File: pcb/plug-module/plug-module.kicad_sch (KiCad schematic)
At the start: 15 parts, among them J1 Conn_01x10_Pin, J2 Conn_01x04_Pin, J3 Conn_01x15_Socket, J4 Conn_01x04_Pin, J5 Conn_01x10_Pin, Q1 BS170, U1 74HC688, U2 74AHC1G08, U3 74HC595

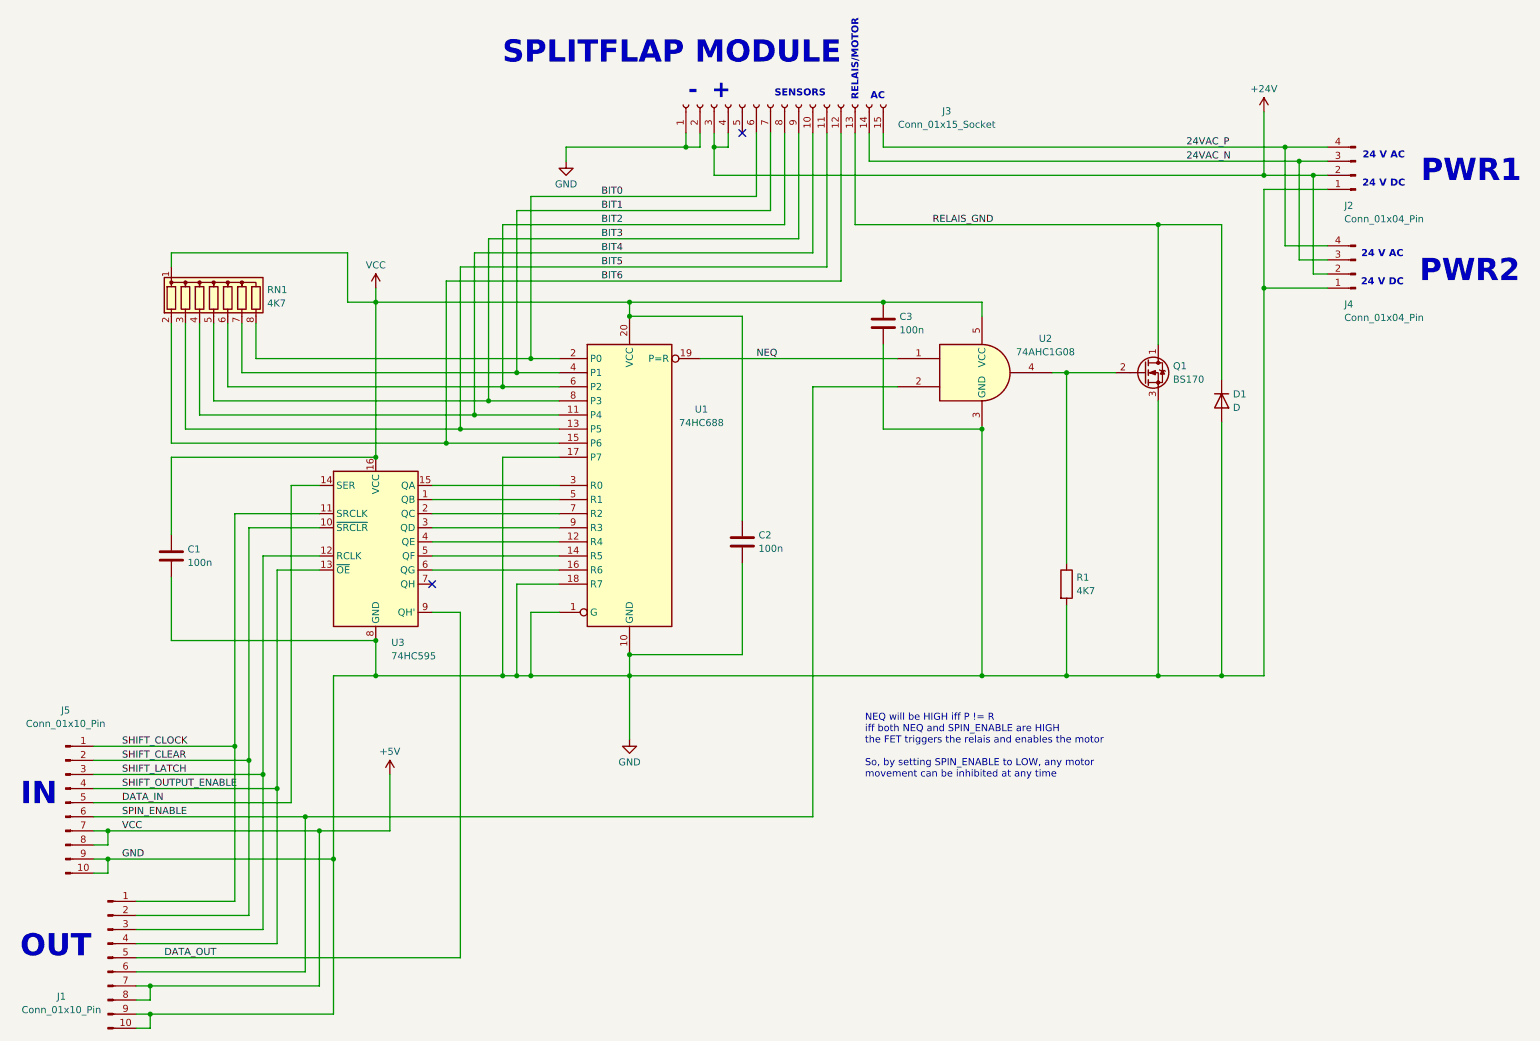
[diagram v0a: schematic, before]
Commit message: plug module improvements (soldering)
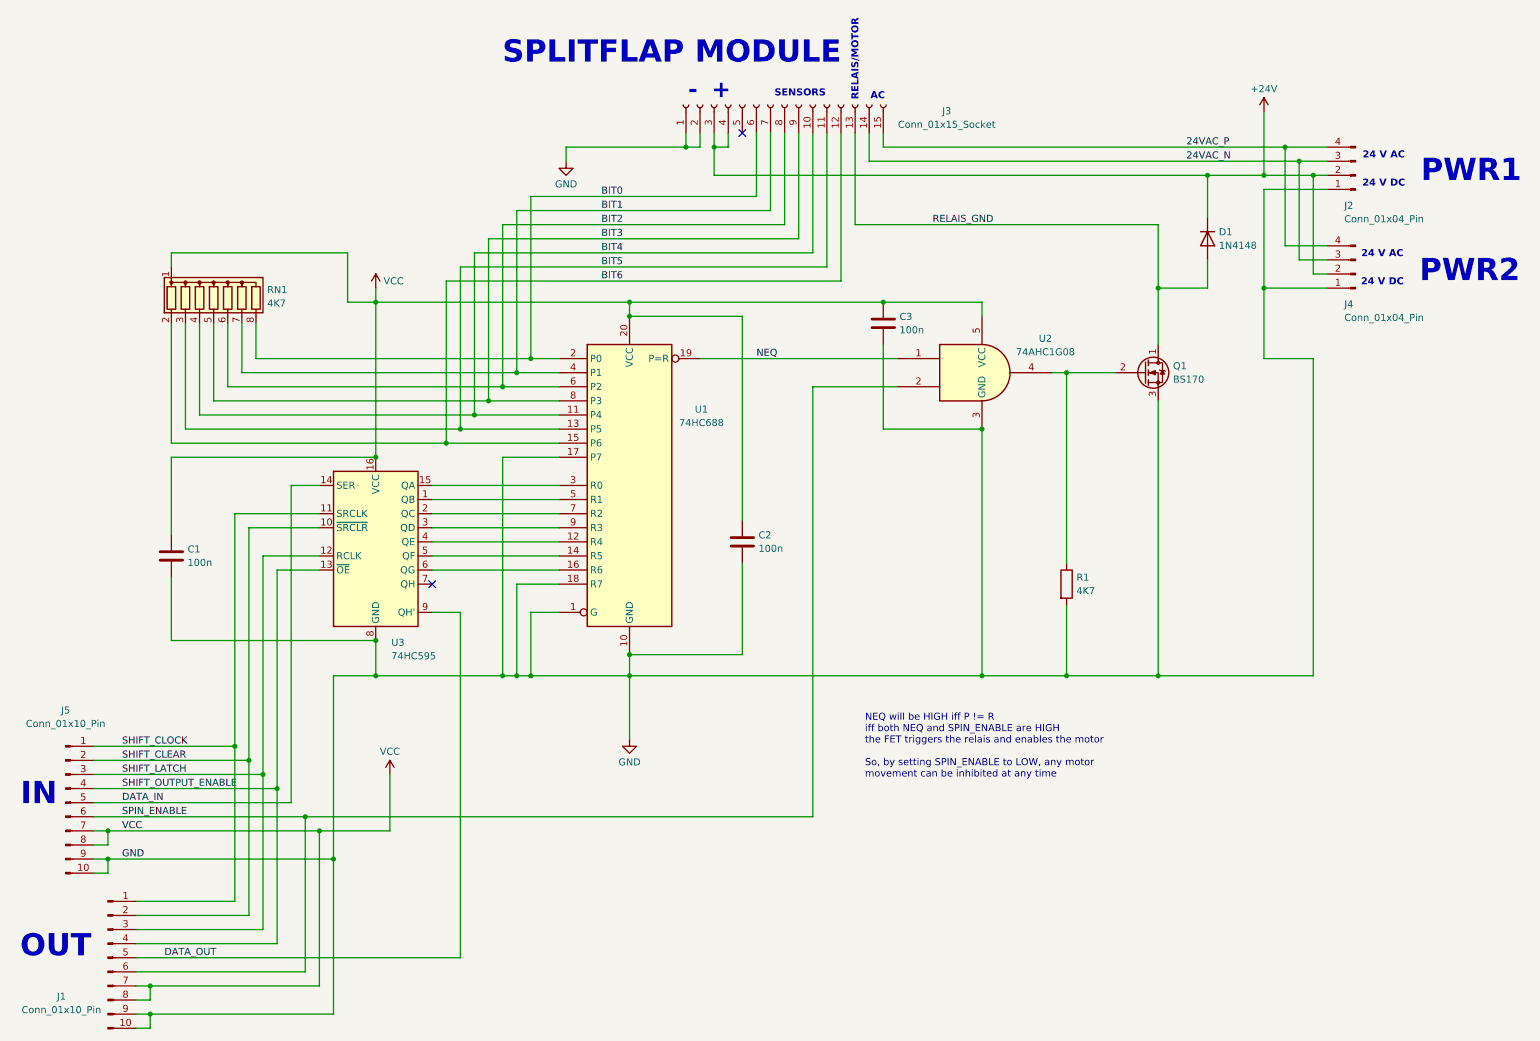
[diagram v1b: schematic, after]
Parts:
- removed D1: D, Diode_THT:D_DO-15_P10.16mm_Horizontal, symbol Device:D
- added D1: 1N4148, Diode_THT:D_T-1_P5.08mm_Horizontal, symbol Diode:1N4148
- U2: footprint Package_TO_SOT_SMD:SOT-353_SC-70-5_Handsoldering -> JS_Local:TSSOP-5_Handsoldering
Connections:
- net +24V: now also D1.1 (K)
- net RELAIS_GND: now also D1.2 (A)
- net +5V renamed VCC
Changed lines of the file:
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@@
 	)
 	(junction
-		(at 218.44 50.8)
-		(diameter 0)
-		(color 0 0 0 0)
-	)
-	(junction
 		(at 243.84 39.37)
 		(diameter 0)
@@
 	)
 	(junction
-		(at 237.49 62.23)
-		(diameter 0)
-		(color 0 0 0 0)
-	)
-	(junction
 		(at 168.91 64.77)
 		(diameter 0)
@@
 	)
 	(junction
-		(at 218.44 132.08)
+		(at 237.49 62.23)
 		(diameter 0)
 		(color 0 0 0 0)
 	)
 	(junction
-		(at 95.25 85.09)
+		(at 218.44 132.08)
 		(diameter 0)
 		(color 0 0 0 0)
 	)
 	(junction
-		(at 77.47 132.08)
+		(at 95.25 85.09)
 		(diameter 0)
 		(color 0 0 0 0)
 	)
 	(junction
-		(at 229.87 132.08)
+		(at 77.47 132.08)
 		(diameter 0)
 		(color 0 0 0 0)
@@
 	)
 	(junction
+		(at 227.33 41.91)
+		(diameter 0)
+		(color 0 0 0 0)
+	)
+	(junction
 		(at 54.61 147.32)
 		(diameter 0)
@@
 	)
 	(junction
+		(at 218.44 62.23)
+		(diameter 0)
+		(color 0 0 0 0)
+	)
+	(junction
 		(at 138.43 36.83)
 		(diameter 0)
@@
 	(wire
 		(pts
-			(xy 229.87 86.36) (xy 229.87 132.08)
-		)
-		(stroke
-			(width 0)
-			(type default)
-		)
-	)
-	(wire
-		(pts
 			(xy 100.33 80.01) (xy 110.49 80.01)
 		)
@@
 	(wire
 		(pts
-			(xy 218.44 50.8) (xy 218.44 72.39)
+			(xy 218.44 50.8) (xy 218.44 62.23)
 		)
 		(stroke
@@
 	(wire
 		(pts
-			(xy 77.47 62.23) (xy 77.47 64.77)
+			(xy 218.44 62.23) (xy 218.44 72.39)
 		)
 		(stroke
@@
 	(wire
 		(pts
-			(xy 97.79 82.55) (xy 110.49 82.55)
+			(xy 77.47 62.23) (xy 77.47 64.77)
 		)
 		(stroke
@@
 	(wire
 		(pts
-			(xy 218.44 50.8) (xy 229.87 50.8)
+			(xy 97.79 82.55) (xy 110.49 82.55)
 		)
 		(stroke
@@
 	(wire
 		(pts
+			(xy 227.33 41.91) (xy 227.33 49.53)
+		)
+		(stroke
+			(width 0)
+			(type default)
+		)
+	)
+	(wire
+		(pts
 			(xy 34.29 182.88) (xy 92.71 182.88)
 		)
@@
 	(wire
 		(pts
+			(xy 218.44 62.23) (xy 227.33 62.23)
+		)
+		(stroke
+			(width 0)
+			(type default)
+		)
+	)
+	(wire
+		(pts
 			(xy 186.69 87.63) (xy 168.91 87.63)
 		)
@@
 	(wire
 		(pts
-			(xy 229.87 50.8) (xy 229.87 78.74)
-		)
-		(stroke
-			(width 0)
-			(type default)
-		)
-	)
-	(wire
-		(pts
 			(xy 133.35 34.29) (xy 133.35 36.83)
 		)
@@
 	(wire
 		(pts
-			(xy 138.43 41.91) (xy 237.49 41.91)
+			(xy 138.43 41.91) (xy 227.33 41.91)
 		)
 		(stroke
@@
 	(wire
 		(pts
+			(xy 237.49 62.23) (xy 237.49 74.93)
+		)
+		(stroke
+			(width 0)
+			(type default)
+		)
+	)
+	(wire
+		(pts
 			(xy 140.97 34.29) (xy 140.97 36.83)
 		)
@@
 	(wire
 		(pts
-			(xy 229.87 132.08) (xy 237.49 132.08)
+			(xy 218.44 132.08) (xy 246.38 132.08)
 		)
 		(stroke
@@
 	(wire
 		(pts
+			(xy 227.33 41.91) (xy 237.49 41.91)
+		)
+		(stroke
+			(width 0)
+			(type default)
+		)
+	)
+	(wire
+		(pts
 			(xy 36.83 187.96) (xy 36.83 190.5)
 		)
@@
 	(wire
 		(pts
-			(xy 146.05 34.29) (xy 146.05 45.72)
+			(xy 227.33 62.23) (xy 227.33 57.15)
 		)
 		(stroke
@@
 	(wire
 		(pts
-			(xy 218.44 132.08) (xy 229.87 132.08)
+			(xy 146.05 34.29) (xy 146.05 45.72)
 		)
 		(stroke
@@
 	(wire
 		(pts
+			(xy 246.38 74.93) (xy 246.38 132.08)
+		)
+		(stroke
+			(width 0)
+			(type default)
+		)
+	)
+	(wire
+		(pts
 			(xy 26.67 144.78) (xy 52.07 144.78)
 		)
@@
 	(wire
 		(pts
-			(xy 168.91 64.77) (xy 186.69 64.77)
+			(xy 237.49 74.93) (xy 246.38 74.93)
 		)
 		(stroke
@@
 	(wire
 		(pts
-			(xy 95.25 85.09) (xy 110.49 85.09)
+			(xy 168.91 64.77) (xy 186.69 64.77)
 		)
 		(stroke
@@
 	(wire
 		(pts
-			(xy 110.49 92.71) (xy 100.33 92.71)
+			(xy 95.25 85.09) (xy 110.49 85.09)
 		)
 		(stroke
@@
 	(wire
 		(pts
-			(xy 45.72 85.09) (xy 45.72 68.58)
+			(xy 110.49 92.71) (xy 100.33 92.71)
 		)
 		(stroke
@@
 	(wire
 		(pts
-			(xy 237.49 62.23) (xy 237.49 132.08)
+			(xy 45.72 85.09) (xy 45.72 68.58)
 		)
 		(stroke
@@
 		)
 		(property "Value" "VCC"
-			(at 77.47 58.0969 0)
+			(at 78.867 60.96 0)
 			(effects
 				(font
 					(size 1.27 1.27)
 				)
+				(justify left)
 			)
 		)
@@
 	)
 	(symbol
-		(lib_id "Device:D")
-		(at 229.87 82.55 270)
-		(unit 1)
-		(exclude_from_sim no)
-		(in_bom yes)
-		(on_board yes)
-		(dnp no)
-		(fields_autoplaced yes)
-		(property "Reference" "D1"
-			(at 231.902 81.3378 90)
-			(effects
-				(font
-					(size 1.27 1.27)
-				)
-				(justify left)
-			)
-		)
-		(property "Value" "D"
-			(at 231.902 83.7621 90)
-			(effects
-				(font
-					(size 1.27 1.27)
-				)
-				(justify left)
-			)
-		)
-		(property "Footprint" "Diode_THT:D_DO-15_P10.16mm_Horizontal"
-			(at 229.87 82.55 0)
-			(effects
-				(font
-					(size 1.27 1.27)
-				)
-				(hide yes)
-			)
-		)
-		(property "Datasheet" "~"
-			(at 229.87 82.55 0)
-			(effects
-				(font
-					(size 1.27 1.27)
-				)
-				(hide yes)
-			)
-		)
-		(property "Description" "Diode"
-			(at 229.87 82.55 0)
-			(effects
-				(font
-					(size 1.27 1.27)
-				)
-				(hide yes)
-			)
-		)
-		(property "Sim.Device" "D"
-			(at 229.87 82.55 0)
-			(effects
-				(font
-					(size 1.27 1.27)
-				)
-				(hide yes)
-			)
-		)
-		(property "Sim.Pins" "1=K 2=A"
-			(at 229.87 82.55 0)
-			(effects
-				(font
-					(size 1.27 1.27)
-				)
-				(hide yes)
-			)
-		)
-		(pin "1"
-		)
-		(pin "2"
-		)
-		(instances
-			(project ""
-				(path "/7d33117e-4f7b-4167-8883-44198fec4073"
-					(reference "D1")
-					(unit 1)
-				)
-			)
-		)
-	)
-	(symbol
 		(lib_id "74xGxx:74AHC1G08")
 		(at 186.69 77.47 0)
@@
 			)
 		)
-		(property "Footprint" "Package_TO_SOT_SMD:SOT-353_SC-70-5_Handsoldering"
+		(property "Footprint" "JS_Local:TSSOP-5_Handsoldering"
 			(at 186.69 77.47 0)
 			(effects
@@
 			)
 		)
-		(property "Value" "+5V"
+		(property "Value" "VCC"
 			(at 80.01 145.7269 0)
 			(effects
@@
 					(unit 1)
 				)
+			)
+		)
+	)
+	(symbol
+		(lib_id "Diode:1N4148")
+		(at 227.33 53.34 270)
+		(unit 1)
+		(exclude_from_sim no)
+		(in_bom yes)
+		(on_board yes)
+		(dnp no)
+		(fields_autoplaced yes)
+		(property "Reference" "D1"
+			(at 229.362 52.1278 90)
+			(effects
+				(font
+					(size 1.27 1.27)
+				)
+				(justify left)
+			)
+		)
+		(property "Value" "1N4148"
+			(at 229.362 54.5521 90)
+			(effects
+				(font
+					(size 1.27 1.27)
+				)
+				(justify left)
+			)
+		)
+		(property "Footprint" "Diode_THT:D_T-1_P5.08mm_Horizontal"
+			(at 227.33 53.34 0)
+			(effects
+				(font
+					(size 1.27 1.27)
+				)
+				(hide yes)
+			)
+		)
+		(property "Datasheet" "https://assets.nexperia.com/documents/data-sheet/1N4148_1N4448.pdf"
+			(at 227.33 53.34 0)
+			(effects
+				(font
+					(size 1.27 1.27)
+				)
+				(hide yes)
+			)
+		)
+		(property "Description" "100V 0.15A standard switching diode, DO-35"
+			(at 227.33 53.34 0)
+			(effects
+				(font
+					(size 1.27 1.27)
+				)
+				(hide yes)
+			)
+		)
+		(property "Sim.Device" "D"
+			(at 227.33 53.34 0)
+			(effects
+				(font
+					(size 1.27 1.27)
+				)
+				(hide yes)
+			)
+		)
+		(property "Sim.Pins" "1=K 2=A"
+			(at 227.33 53.34 0)
+			(effects
+				(font
+					(size 1.27 1.27)
+				)
+				(hide yes)
+			)
+		)
+		(pin "2"
+		)
+		(pin "1"
+		)
+		(instances
+			(project ""
+				(path "/7d33117e-4f7b-4167-8883-44198fec4073"
+					(reference "D1")
+					(unit 1)
+				)

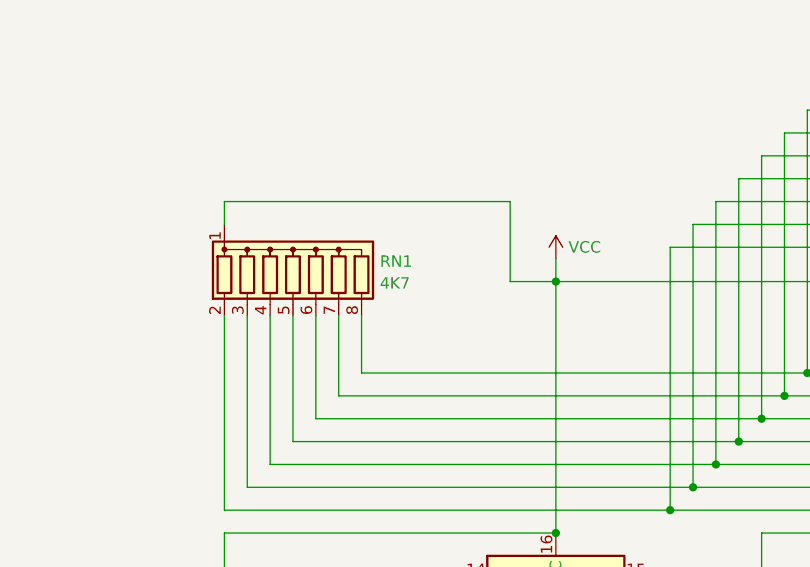
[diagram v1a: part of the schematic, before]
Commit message: first version firmware, rounded corners
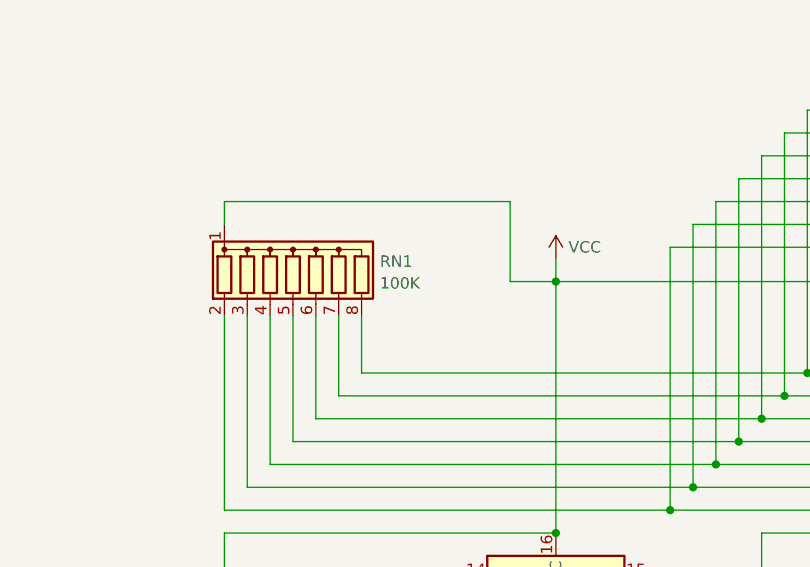
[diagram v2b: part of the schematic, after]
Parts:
- RN1: value 4K7 -> 100K
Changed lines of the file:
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@@
 			)
 		)
-		(property "Value" "4K7"
+		(property "Value" "100K"
 			(at 57.912 64.9661 0)
 			(effects
